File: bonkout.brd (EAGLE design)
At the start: 45.5 x 38.6 mm, 8 parts

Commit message: Add files via upload
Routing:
- net S$12: track 37.3 -> 25.3 mm
- net S$17: track 34.6 -> 27.1 mm
- net S$2: track 28.9 -> 23.6 mm
- net S$13: track 27.8 -> 24.6 mm
- net S$1: track 25.8 -> 24.1 mm
- net S$16: track 28.0 -> 27.2 mm
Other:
- board text added: "TURN OFF PRINTER BEFORE PLUGGING OR UNPLUGGING. FAILING TO DO SO CAN CAUSE DAMAGE TO BOARDS OR PARTS"
- board text added: "Wire2Hotend v1"
- board text removed: "Wire2Hotend v0.5"

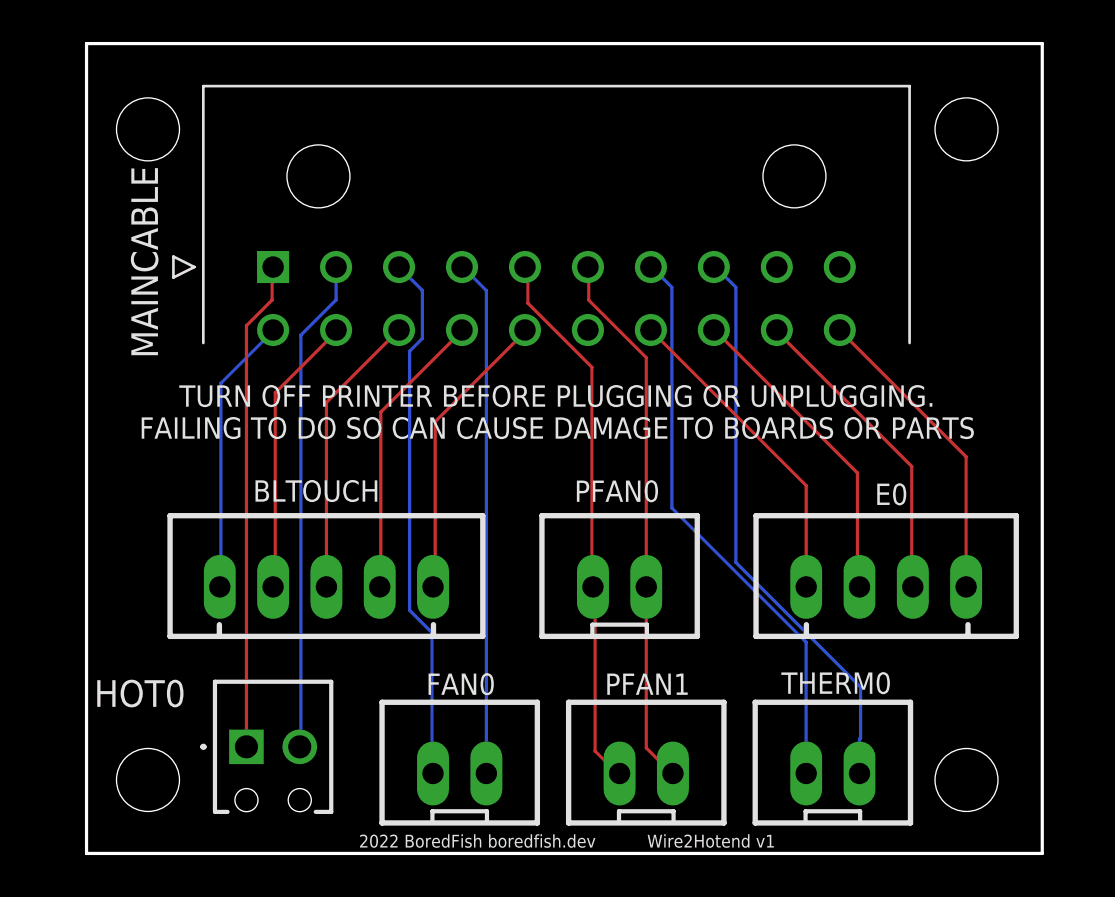
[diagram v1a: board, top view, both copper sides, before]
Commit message: Wire2Hotend
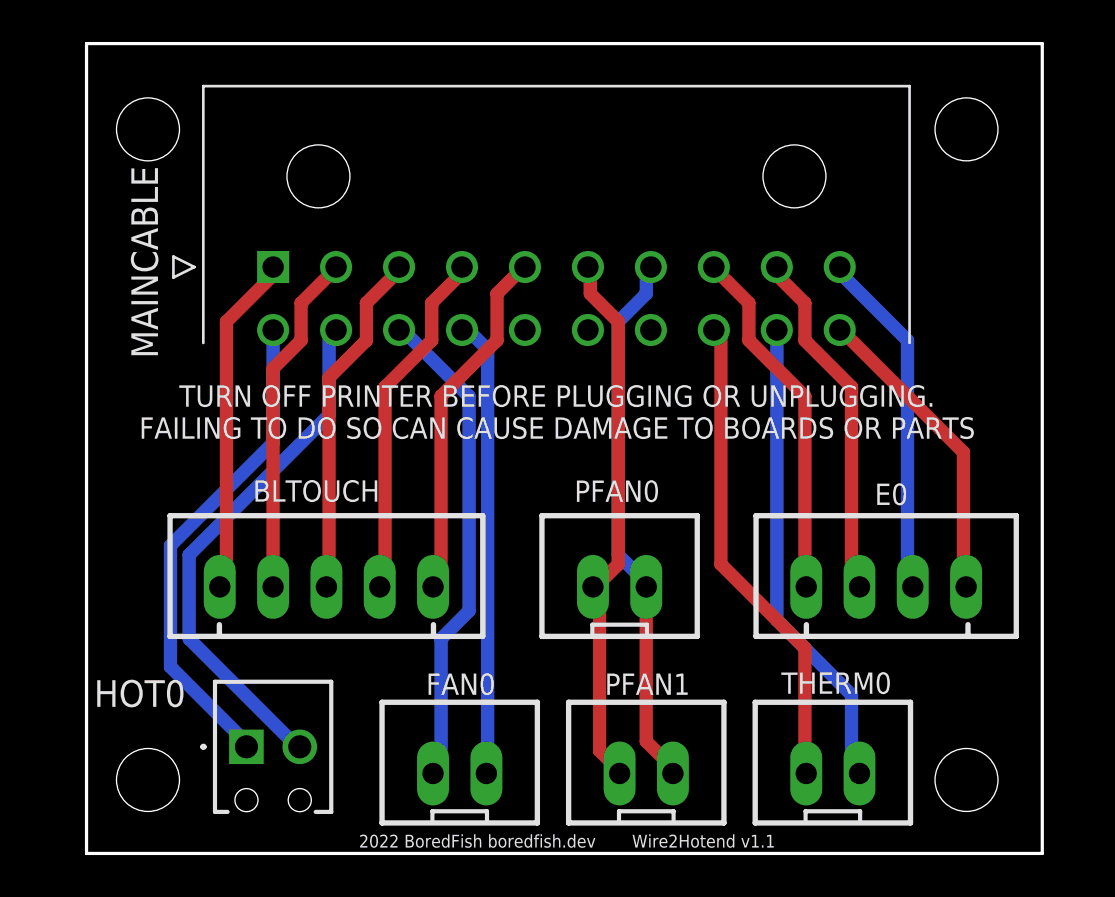
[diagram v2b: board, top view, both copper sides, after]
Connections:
- removed net S$12: FAN0.1, MAINCABLE.3
- removed net S$2: HOT0.2, MAINCABLE.2
- new net S$20: HOT0.2, MAINCABLE.12
- new net S$21: FAN0.1, MAINCABLE.13
- net S$1: now also BLTOUCH.1; no longer HOT0.1
- net S$10: now also FAN0.2, MAINCABLE.14; no longer E0.2, MAINCABLE.18
- net S$11: now also MAINCABLE.8; no longer MAINCABLE.17
- net S$13: now also E0.2, MAINCABLE.9; no longer FAN0.2, MAINCABLE.4
- net S$14: now also E0.3, MAINCABLE.10; no longer MAINCABLE.5, PFAN0.1, PFAN1.1
- net S$15: now also E0.4, MAINCABLE.20; no longer MAINCABLE.6, PFAN0.2, PFAN1.2
- net S$16: now also MAINCABLE.18; no longer MAINCABLE.7
- net S$17: now also MAINCABLE.19; no longer MAINCABLE.8
- net S$3: now also BLTOUCH.3, MAINCABLE.3; no longer BLTOUCH.1, MAINCABLE.11
- net S$4: now also MAINCABLE.2; no longer MAINCABLE.12
- net S$5: now also BLTOUCH.4, MAINCABLE.4; no longer BLTOUCH.3, MAINCABLE.13
- net S$6: now also BLTOUCH.5, MAINCABLE.5; no longer BLTOUCH.4, MAINCABLE.14
- net S$7: now also HOT0.1, MAINCABLE.11; no longer BLTOUCH.5, MAINCABLE.15
- net S$8: now also MAINCABLE.6, PFAN0.1, PFAN1.1; no longer E0.4, MAINCABLE.20
- net S$9: now also MAINCABLE.7, PFAN0.2, PFAN1.2; no longer E0.3, MAINCABLE.19
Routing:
- net S$12: track 25.3 -> 0.00 mm
- net S$20: track 0.00 -> 25.1 mm
- net S$2: track 23.6 -> 0.00 mm
- net S$21: track 0.00 -> 23.4 mm
- net S$15: track 25.8 -> 14.7 mm
- net S$8: track 14.7 -> 25.8 mm
- net S$9: track 14.9 -> 25.9 mm
- net S$14: track 26.1 -> 16.7 mm
- net S$7: track 14.1 -> 23.4 mm
- net S$1: track 24.1 -> 16.3 mm
- net S$13: track 24.6 -> 16.9 mm
- net S$10: track 15.1 -> 21.8 mm
- net S$17: track 27.1 -> 22.8 mm
- net S$16: track 27.2 -> 23.1 mm
- net S$3: track 13.3 -> 16.6 mm
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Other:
- board text added: "Wire2Hotend v1.1"
- board text removed: "Wire2Hotend v1"

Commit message: Add files via upload
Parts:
- added LED: (no value), Rembrandt Electronics - JST XH Connectors v1-0:JST-XH-03-PACKAGE-LONG-PAD
- MAINCABLE: device SamacSys_Parts:43045-20YY -> SamacSys_Parts:43045-20(00,01,02,10)
- moved BLTOUCH 3.17 mm to (8.26, 12.7)
- moved PFAN0 2.54 mm to (27.9, 12.7)
- moved E0 0.84 mm to (38.9, 12.7)
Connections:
- new net S$12: LED.2, MAINCABLE.16
- new net S$18: LED.1, MAINCABLE.15
- new net S$2: LED.3, MAINCABLE.17
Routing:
- net S$18: track 0.00 -> 16.2 mm
- net S$12: track 0.00 -> 12.9 mm
- net S$2: track 0.00 -> 11.5 mm
- net S$6: track 17.2 -> 28.6 mm
- net S$20: track 25.1 -> 22.9 mm
- net S$7: track 23.4 -> 25.2 mm
- net S$21: track 23.4 -> 21.9 mm
- net S$1: track 16.3 -> 17.7 mm
- net S$5: track 16.9 -> 18.2 mm
- net S$3: track 16.6 -> 18.0 mm
- net S$4: track 16.5 -> 17.8 mm
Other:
- board text added: "Wire2Hotend v1.5"
- board text removed: "Wire2Hotend v1.1"
